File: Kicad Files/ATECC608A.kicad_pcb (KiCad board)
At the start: 2 copper layers, 7 parts, among them J1 Conn_01x04, U1 ATECC608A-SSHDA

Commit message: Change name LED1 and netlist
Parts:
- renumbered D1 to ON
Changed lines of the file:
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@@
-(kicad_pcb (version 20171130) (host pcbnew "(5.1.4-0-10_14)")
+(kicad_pcb (version 20171130) (host pcbnew "(5.1.4)-1")
   (general
     (thickness 1.6)
@@
     (solder_mask_min_width 0.25)
     (aux_axis_origin 0 0)
-    (visible_elements FFFFFF7F)
+    (visible_elements 7FFFFFFF)
     (pcbplotparams
       (layerselection 0x010fc_ffffffff)
@@
   (net 1 +3V3)
   (net 2 GND)
-  (net 3 "Net-(D1-Pad1)")
-  (net 4 /SCL)
-  (net 5 /SDA)
+  (net 3 /SCL)
+  (net 4 /SDA)
+  (net 5 "Net-(ON1-Pad1)")
   (net_class Default "This is the default net class."
     (clearance 0.2)
@@
     (add_net /SDA)
     (add_net GND)
-    (add_net "Net-(D1-Pad1)")
-  )
-  (module Capacitor_SMD:C_0805_2012Metric_Pad1.15x1.40mm_HandSolder (layer F.Cu)
-    (at 164.275 32.525 180)
-    (descr "Capacitor SMD 0805 (2012 Metric), square (rectangular) end terminal, IPC_7351 nominal with elongated pad for handsoldering. (Body size source: https://docs.google.com/spreadsheets/d/1BsfQQcO9C6DZCsRaXUlFlo91Tg2WpOkGARC1WS5S8t0/edit?usp=sharing), generated with kicad-footprint-generator")
-    (tags "capacitor handsolder")
-    (attr smd)
-    (fp_text reference C1 (at 0 -1.65) (layer F.SilkS)
-      (effects (font (size 1 1) (thickness 0.15)))
-    )
-    (fp_text value 0.1uF (at 0 1.65) (layer F.Fab)
-      (effects (font (size 1 1) (thickness 0.15)))
-    )
-    (fp_line (start -1 0.6) (end -1 -0.6) (layer F.Fab) (width 0.1))
-    (fp_line (start -1 -0.6) (end 1 -0.6) (layer F.Fab) (width 0.1))
-    (fp_line (start 1 -0.6) (end 1 0.6) (layer F.Fab) (width 0.1))
-    (fp_line (start 1 0.6) (end -1 0.6) (layer F.Fab) (width 0.1))
-    (fp_line (start -0.261252 -0.71) (end 0.261252 -0.71) (layer F.SilkS) (width 0.12))
-    (fp_line (start -0.261252 0.71) (end 0.261252 0.71) (layer F.SilkS) (width 0.12))
-    (fp_line (start -1.85 0.95) (end -1.85 -0.95) (layer F.CrtYd) (width 0.05))
-    (fp_line (start -1.85 -0.95) (end 1.85 -0.95) (layer F.CrtYd) (width 0.05))
-    (fp_line (start 1.85 -0.95) (end 1.85 0.95) (layer F.CrtYd) (width 0.05))
-    (fp_line (start 1.85 0.95) (end -1.85 0.95) (layer F.CrtYd) (width 0.05))
-    (fp_text user %R (at 0 0) (layer F.Fab)
-      (effects (font (size 0.5 0.5) (thickness 0.08)))
-    )
-    (pad 1 smd roundrect (at -1.025 0 180) (size 1.15 1.4) (layers F.Cu F.Paste F.Mask) (roundrect_rratio 0.217391)
-      (net 1 +3V3))
-    (pad 2 smd roundrect (at 1.025 0 180) (size 1.15 1.4) (layers F.Cu F.Paste F.Mask) (roundrect_rratio 0.217391)
-      (net 2 GND))
-    (model ${KISYS3DMOD}/Capacitor_SMD.3dshapes/C_0805_2012Metric.wrl
-      (at (xyz 0 0 0))
-      (scale (xyz 1 1 1))
-      (rotate (xyz 0 0 0))
-    )
+    (add_net "Net-(ON1-Pad1)")
   )
   (module LED_SMD:LED_0805_2012Metric_Pad1.15x1.40mm_HandSolder (layer F.Cu)
@@
     (tags "LED handsolder")
     (attr smd)
-    (fp_text reference D1 (at 0 -1.65) (layer F.SilkS)
+    (fp_text reference ON (at 0 -1.65) (layer F.SilkS)
       (effects (font (size 1 1) (thickness 0.15)))
     )
@@
     )
     (pad 1 smd roundrect (at -1.025 0) (size 1.15 1.4) (layers F.Cu F.Paste F.Mask) (roundrect_rratio 0.217391)
-      (net 3 "Net-(D1-Pad1)"))
+      (net 5 "Net-(ON1-Pad1)"))
     (pad 2 smd roundrect (at 1.025 0) (size 1.15 1.4) (layers F.Cu F.Paste F.Mask) (roundrect_rratio 0.217391)
       (net 1 +3V3))
     (model ${KISYS3DMOD}/LED_SMD.3dshapes/LED_0805_2012Metric.wrl
+      (at (xyz 0 0 0))
+      (scale (xyz 1 1 1))
+      (rotate (xyz 0 0 0))
+    )
+  )
+  (module Capacitor_SMD:C_0805_2012Metric_Pad1.15x1.40mm_HandSolder (layer F.Cu)
+    (at 164.275 32.525 180)
+    (descr "Capacitor SMD 0805 (2012 Metric), square (rectangular) end terminal, IPC_7351 nominal with elongated pad for handsoldering. (Body size source: https://docs.google.com/spreadsheets/d/1BsfQQcO9C6DZCsRaXUlFlo91Tg2WpOkGARC1WS5S8t0/edit?usp=sharing), generated with kicad-footprint-generator")
+    (tags "capacitor handsolder")
+    (attr smd)
+    (fp_text reference C1 (at 0 -1.65) (layer F.SilkS)
+      (effects (font (size 1 1) (thickness 0.15)))
+    )
+    (fp_text value 0.1uF (at 0 1.65) (layer F.Fab)
+      (effects (font (size 1 1) (thickness 0.15)))
+    )
+    (fp_line (start -1 0.6) (end -1 -0.6) (layer F.Fab) (width 0.1))
+    (fp_line (start -1 -0.6) (end 1 -0.6) (layer F.Fab) (width 0.1))
+    (fp_line (start 1 -0.6) (end 1 0.6) (layer F.Fab) (width 0.1))
+    (fp_line (start 1 0.6) (end -1 0.6) (layer F.Fab) (width 0.1))
+    (fp_line (start -0.261252 -0.71) (end 0.261252 -0.71) (layer F.SilkS) (width 0.12))
+    (fp_line (start -0.261252 0.71) (end 0.261252 0.71) (layer F.SilkS) (width 0.12))
+    (fp_line (start -1.85 0.95) (end -1.85 -0.95) (layer F.CrtYd) (width 0.05))
+    (fp_line (start -1.85 -0.95) (end 1.85 -0.95) (layer F.CrtYd) (width 0.05))
+    (fp_line (start 1.85 -0.95) (end 1.85 0.95) (layer F.CrtYd) (width 0.05))
+    (fp_line (start 1.85 0.95) (end -1.85 0.95) (layer F.CrtYd) (width 0.05))
+    (fp_text user %R (at 0 0) (layer F.Fab)
+      (effects (font (size 0.5 0.5) (thickness 0.08)))
+    )
+    (pad 1 smd roundrect (at -1.025 0 180) (size 1.15 1.4) (layers F.Cu F.Paste F.Mask) (roundrect_rratio 0.217391)
+      (net 1 +3V3))
+    (pad 2 smd roundrect (at 1.025 0 180) (size 1.15 1.4) (layers F.Cu F.Paste F.Mask) (roundrect_rratio 0.217391)
+      (net 2 GND))
+    (model ${KISYS3DMOD}/Capacitor_SMD.3dshapes/C_0805_2012Metric.wrl
       (at (xyz 0 0 0))
       (scale (xyz 1 1 1))
@@
       (net 2 GND))
     (pad 3 thru_hole oval (at 0 5.08 90) (size 1.7 1.7) (drill 1) (layers *.Cu *.Mask)
-      (net 4 /SCL))
+      (net 3 /SCL))
     (pad 4 thru_hole oval (at 0 7.62 90) (size 1.7 1.7) (drill 1) (layers *.Cu *.Mask)
-      (net 5 /SDA))
+      (net 4 /SDA))
     (model ${KISYS3DMOD}/Connector_PinHeader_2.54mm.3dshapes/PinHeader_1x04_P2.54mm_Vertical.wrl
       (at (xyz 0 0 0))
@@
     )
     (pad 1 smd roundrect (at -1.025 0) (size 1.15 1.4) (layers F.Cu F.Paste F.Mask) (roundrect_rratio 0.217391)
-      (net 3 "Net-(D1-Pad1)"))
+      (net 5 "Net-(ON1-Pad1)"))
     (pad 2 smd roundrect (at 1.025 0) (size 1.15 1.4) (layers F.Cu F.Paste F.Mask) (roundrect_rratio 0.217391)
       (net 2 GND))
@@
       (net 2 GND))
     (pad 5 smd roundrect (at 2.475 1.905) (size 1.95 0.6) (layers F.Cu F.Paste F.Mask) (roundrect_rratio 0.25)
-      (net 5 /SDA))
+      (net 4 /SDA))
     (pad 6 smd roundrect (at 2.475 0.635) (size 1.95 0.6) (layers F.Cu F.Paste F.Mask) (roundrect_rratio 0.25)
-      (net 4 /SCL))
+      (net 3 /SCL))
     (pad 7 smd roundrect (at 2.475 -0.635) (size 1.95 0.6) (layers F.Cu F.Paste F.Mask) (roundrect_rratio 0.25))
     (pad 8 smd roundrect (at 2.475 -1.905) (size 1.95 0.6) (layers F.Cu F.Paste F.Mask) (roundrect_rratio 0.25)
@@
     (fp_line (start -1 0.6) (end -1 -0.6) (layer F.Fab) (width 0.1))
     (pad 2 smd roundrect (at 1.025 0 270) (size 1.15 1.4) (layers F.Cu F.Paste F.Mask) (roundrect_rratio 0.217391)
-      (net 4 /SCL))
+      (net 3 /SCL))
     (pad 1 smd roundrect (at -1.025 0 270) (size 1.15 1.4) (layers F.Cu F.Paste F.Mask) (roundrect_rratio 0.217391)
       (net 1 +3V3))
@@
       (net 1 +3V3))
     (pad 2 smd roundrect (at 1.025 0 270) (size 1.15 1.4) (layers F.Cu F.Paste F.Mask) (roundrect_rratio 0.217391)
-      (net 5 /SDA))
+      (net 4 /SDA))
     (model ${KISYS3DMOD}/Resistor_SMD.3dshapes/R_0805_2012Metric.wrl
       (at (xyz 0 0 0))

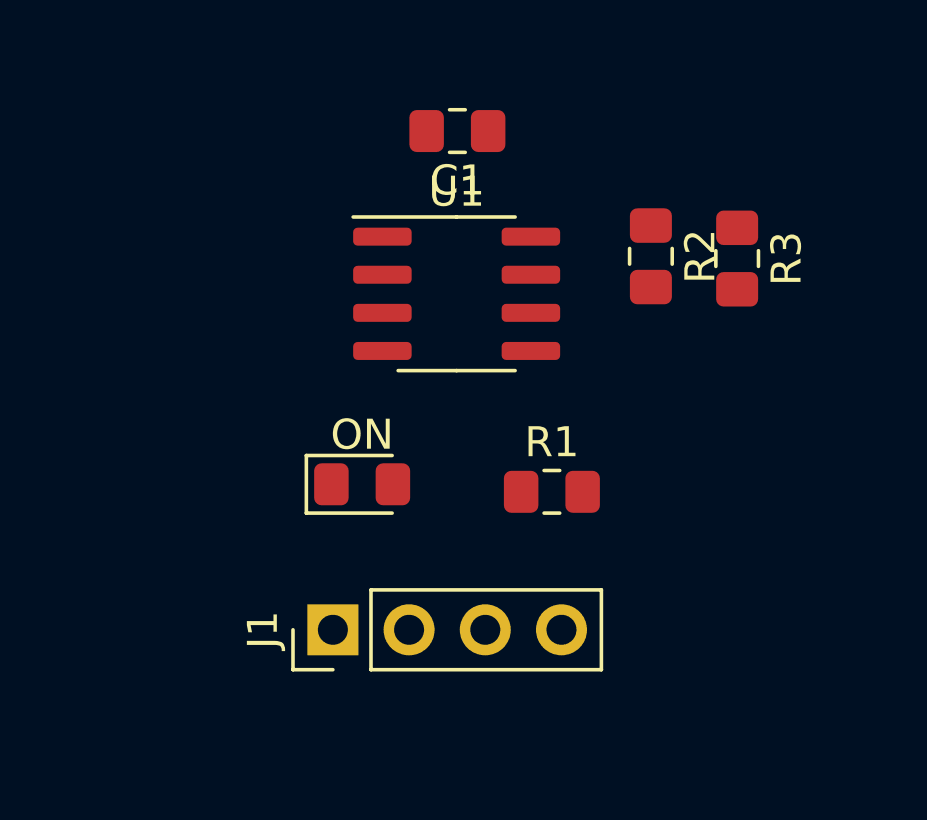
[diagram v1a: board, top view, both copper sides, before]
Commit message: Desing rules and  contour pcb
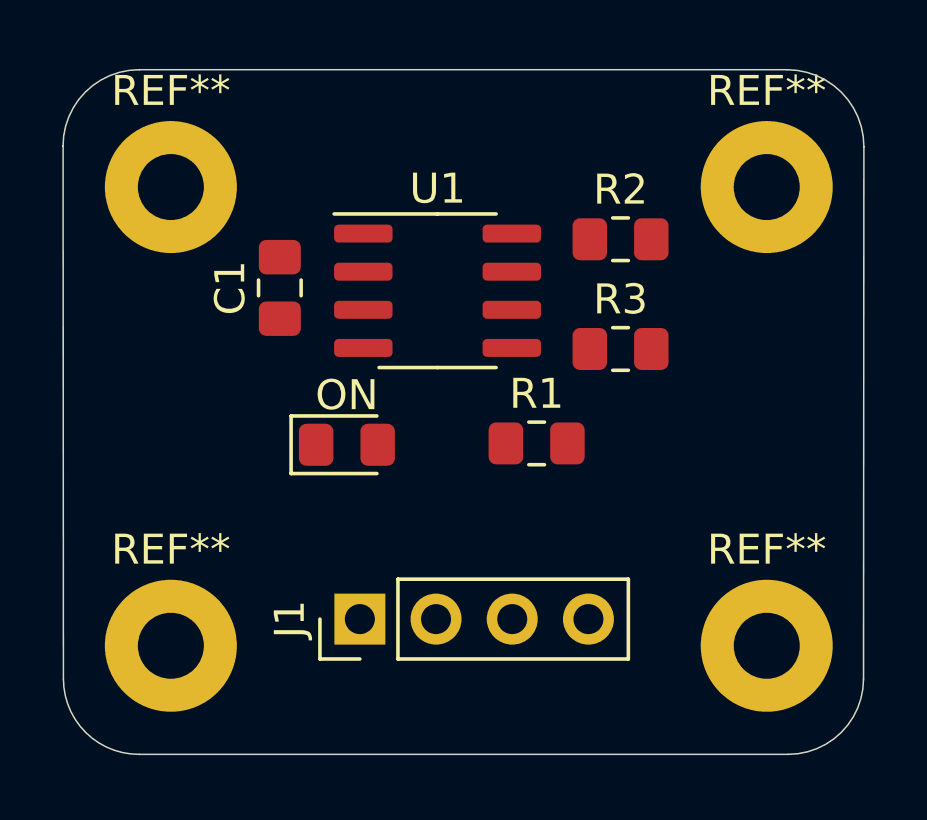
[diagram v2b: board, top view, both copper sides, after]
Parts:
- added REF**: MountingHole_2.2mm_M2_Pad, MountingHole:MountingHole_2.2mm_M2_Pad, F.Cu at (154.7, 34.4)
- added REF**: MountingHole_2.2mm_M2_Pad, MountingHole:MountingHole_2.2mm_M2_Pad, F.Cu at (154.7, 49.7)
- added REF**: MountingHole_2.2mm_M2_Pad, MountingHole:MountingHole_2.2mm_M2_Pad, F.Cu at (174.6, 49.7)
- added REF**: MountingHole_2.2mm_M2_Pad, MountingHole:MountingHole_2.2mm_M2_Pad, F.Cu at (174.6, 34.4)
- moved C1 7.90 mm to (158.4, 37.8), turned to 90 degrees
- moved R3 4.92 mm to (169.7, 39.8), turned to 0 degrees
- moved R1 1.69 mm to (166.9, 42.9)
- moved ON 1.41 mm to (160.6, 43.0)
- moved R2 1.16 mm to (169.7, 36.1), turned to 0 degrees
- moved J1 0.97 mm to (161.0, 48.8)
- moved U1 0.64 mm to (163.6, 37.8)
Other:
- board outline added: 26.7 x 22.8 mm
- net class Default: clearance 0.2 -> 0.25; trace_width 0.25 -> 0.3
- net class vcc added: clearance 0.45, trace_width 0.5, via_dia 0.8, via_drill 0.4
- rule trace_clearance: 0.2 -> 0.25

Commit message: add logo EC
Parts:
- added G***: LOGO, Aesthetics:electronic_cats_logo_8x6, F.Cu at (173.5, 43.4)
- moved C1 2.09 mm to (159.7, 39.4)
- moved R1 2.09 mm to (168.3, 44.5)
- moved R3 2.09 mm to (171.1, 41.4)
- moved ON 2.09 mm to (161.9, 44.6)
- moved R2 2.09 mm to (171.1, 37.7)
- moved U1 2.09 mm to (165.0, 39.4)
- moved J1 0.99 mm to (161.0, 49.8)

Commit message: Change of measures
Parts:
- moved REF** 0.20 mm to (174.5, 49.5)
- moved REF** 0.19 mm to (174.6, 34.2)
- moved REF** 0.18 mm to (154.7, 34.2)
- moved REF** 0.14 mm to (154.9, 49.7)

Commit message: accommodation screws
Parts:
- moved REF** 0.27 mm to (154.9, 49.5)
- moved REF** 0.07 mm to (174.4, 49.5)
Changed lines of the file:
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@@
   )
   (module MountingHole:MountingHole_2.2mm_M2_Pad (layer F.Cu)
-    (at 154.8511 49.7459)
+    (at 154.8638 49.4792)
     (descr "Mounting Hole 2.2mm, M2")
     (tags "mounting hole 2.2mm m2")
@@
   )
   (module MountingHole:MountingHole_2.2mm_M2_Pad (layer F.Cu)
-    (at 174.4726 49.5173)
+    (at 174.4091 49.4919)
     (descr "Mounting Hole 2.2mm, M2")
     (tags "mounting hole 2.2mm m2")
@@
     )
   )
+  (dimension 3.8481 (width 0.15) (layer Margin)
+    (gr_text "3.848 mm" (at 181.9067 51.41595 90) (layer Margin)
+      (effects (font (size 1 1) (thickness 0.15)))
+    )
+    (feature1 (pts (xy 174.2059 49.4919) (xy 181.193121 49.4919)))
+    (feature2 (pts (xy 174.2059 53.34) (xy 181.193121 53.34)))
+    (crossbar (pts (xy 180.6067 53.34) (xy 180.6067 49.4919)))
+    (arrow1a (pts (xy 180.6067 49.4919) (xy 181.193121 50.618404)))
+    (arrow1b (pts (xy 180.6067 49.4919) (xy 180.020279 50.618404)))
+    (arrow2a (pts (xy 180.6067 53.34) (xy 181.193121 52.213496)))
+    (arrow2b (pts (xy 180.6067 53.34) (xy 180.020279 52.213496)))
+  )
+  (dimension 3.8481 (width 0.15) (layer Margin)
+    (gr_text "3.848 mm" (at 146.401 51.37785 90) (layer Margin)
+      (effects (font (size 1 1) (thickness 0.15)))
+    )
+    (feature1 (pts (xy 154.9019 49.4538) (xy 147.114579 49.4538)))
+    (feature2 (pts (xy 154.9019 53.3019) (xy 147.114579 53.3019)))
+    (crossbar (pts (xy 147.701 53.3019) (xy 147.701 49.4538)))
+    (arrow1a (pts (xy 147.701 49.4538) (xy 148.287421 50.580304)))
+    (arrow1b (pts (xy 147.701 49.4538) (xy 147.114579 50.580304)))
+    (arrow2a (pts (xy 147.701 53.3019) (xy 148.287421 52.175396)))
+    (arrow2b (pts (xy 147.701 53.3019) (xy 147.114579 52.175396)))
+  )
   (dimension 3.7211 (width 0.15) (layer Margin)
     (gr_text "3.721 mm" (at 153.02865 59.3517) (layer Margin)
@@
     (arrow2b (pts (xy 154.9146 25.8064) (xy 153.788096 26.392821)))
   )
-  (dimension 3.7084 (width 0.15) (layer Margin)
-    (gr_text "3.708 mm" (at 181.2209 51.3969 270) (layer Margin)
-      (effects (font (size 1 1) (thickness 0.15)))
-    )
-    (feature1 (pts (xy 174.4853 53.2511) (xy 180.507321 53.2511)))
-    (feature2 (pts (xy 174.4853 49.5427) (xy 180.507321 49.5427)))
-    (crossbar (pts (xy 179.9209 49.5427) (xy 179.9209 53.2511)))
-    (arrow1a (pts (xy 179.9209 53.2511) (xy 179.334479 52.124596)))
-    (arrow1b (pts (xy 179.9209 53.2511) (xy 180.507321 52.124596)))
-    (arrow2a (pts (xy 179.9209 49.5427) (xy 179.334479 50.669204)))
-    (arrow2b (pts (xy 179.9209 49.5427) (xy 180.507321 50.669204)))
-  )
-  (dimension 3.7592 (width 0.15) (layer Margin)
-    (gr_text "3.759 mm" (at 145.131 51.3715 270) (layer Margin)
-      (effects (font (size 1 1) (thickness 0.15)))
-    )
-    (feature1 (pts (xy 154.9019 53.2511) (xy 145.844579 53.2511)))
-    (feature2 (pts (xy 154.9019 49.4919) (xy 145.844579 49.4919)))
-    (crossbar (pts (xy 146.431 49.4919) (xy 146.431 53.2511)))
-    (arrow1a (pts (xy 146.431 53.2511) (xy 145.844579 52.124596)))
-    (arrow1b (pts (xy 146.431 53.2511) (xy 147.017421 52.124596)))
-    (arrow2a (pts (xy 146.431 49.4919) (xy 145.844579 50.618404)))
-    (arrow2b (pts (xy 146.431 49.4919) (xy 147.017421 50.618404)))
-  )
   (dimension 3.8481 (width 0.15) (layer Margin)

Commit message: initial routeo
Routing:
- net /SCL: track 0.00 -> 34.2 mm, vias 0 -> 1
- net +3V3: track 0.00 -> 32.7 mm
- net /SDA: track 0.00 -> 16.5 mm
- net Net-(ON1-Pad1): track 0.00 -> 9.09 mm
- added copper zone on B.Cu, net GND
- added copper zone on F.Cu, net GND
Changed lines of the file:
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@@
     (thickness 1.6)
     (drawings 21)
-    (tracks 0)
+    (tracks 64)
     (zones 0)
     (modules 12)
@@
   (gr_arc (start 153.67 33.02) (end 153.67 30.48) (angle -90) (layer Edge.Cuts) (width 0.05))
   (gr_arc (start 175.26 33.0454) (end 177.8254 33.0454) (angle -90) (layer Edge.Cuts) (width 0.05))
+  (segment (start 169.850701 37.543401) (end 170.0388 37.7315) (width 0.3) (layer F.Cu) (net 1))
+  (segment (start 167.440001 37.543401) (end 169.850701 37.543401) (width 0.3) (layer F.Cu) (net 1))
+  (segment (start 159.886 49.784) (end 161.036 49.784) (width 0.3) (layer F.Cu) (net 1))
+  (segment (start 159.7063 49.6043) (end 159.886 49.784) (width 0.3) (layer F.Cu) (net 1))
+  (segment (start 162.967 44.5821) (end 162.967 43.0409) (width 0.3) (layer F.Cu) (net 1))
+  (segment (start 162.967 43.0409) (end 162.6578 42.7317) (width 0.3) (layer F.Cu) (net 1))
+  (segment (start 160.0035 42.7317) (end 159.7063 42.4345) (width 0.3) (layer F.Cu) (net 1))
+  (segment (start 160.067 42.7317) (end 160.0035 42.7317) (width 0.3) (layer F.Cu) (net 1))
+  (segment (start 159.7063 42.4345) (end 159.7063 42.7317) (width 0.3) (layer F.Cu) (net 1))
+  (segment (start 159.7063 40.3784) (end 159.7063 42.4345) (width 0.3) (layer F.Cu) (net 1))
+  (segment (start 160.067 42.7317) (end 159.7063 42.7317) (width 0.3) (layer F.Cu) (net 1))
+  (segment (start 159.9552 42.7317) (end 159.7063 42.9806) (width 0.3) (layer F.Cu) (net 1))
+  (segment (start 160.067 42.7317) (end 159.9552 42.7317) (width 0.3) (layer F.Cu) (net 1))
+  (segment (start 159.7063 42.7317) (end 159.7063 42.9806) (width 0.3) (layer F.Cu) (net 1))
+  (segment (start 159.7063 42.9806) (end 159.7063 49.6043) (width 0.3) (layer F.Cu) (net 1))
+  (segment (start 166.365001 37.543401) (end 165.0619 38.846502) (width 0.3) (layer F.Cu) (net 1))
+  (segment (start 167.440001 37.543401) (end 166.365001 37.543401) (width 0.3) (layer F.Cu) (net 1))
+  (segment (start 165.0619 38.846502) (end 165.0619 42.4434) (width 0.3) (layer F.Cu) (net 1))
+  (segment (start 165.0619 42.4434) (end 164.7736 42.7317) (width 0.3) (layer F.Cu) (net 1))
+  (segment (start 162.6578 42.7317) (end 162.3098 42.7317) (width 0.3) (layer F.Cu) (net 1))
+  (segment (start 162.3098 42.7317) (end 160.067 42.7317) (width 0.3) (layer F.Cu) (net 1))
+  (segment (start 162.9963 43.0409) (end 163.3055 42.7317) (width 0.3) (layer F.Cu) (net 1))
+  (segment (start 162.967 43.0409) (end 162.9963 43.0409) (width 0.3) (layer F.Cu) (net 1))
+  (segment (start 164.7736 42.7317) (end 163.3055 42.7317) (width 0.3) (layer F.Cu) (net 1))
+  (segment (start 163.3055 42.7317) (end 162.3098 42.7317) (width 0.3) (layer F.Cu) (net 1))
+  (segment (start 170.0388 40.5891) (end 170.0388 37.7315) (width 0.3) (layer F.Cu) (net 1))
+  (segment (start 170.0388 41.3891) (end 170.0388 40.5891) (width 0.3) (layer F.Cu) (net 1))
+  (via (at 166.1033 42.8498) (size 0.8) (drill 0.4) (layers F.Cu B.Cu) (net 3))
+  (segment (start 166.116 49.784) (end 166.116 42.8625) (width 0.3) (layer B.Cu) (net 3))
+  (segment (start 166.116 42.8625) (end 166.1033 42.8498) (width 0.3) (layer B.Cu) (net 3))
+  (segment (start 166.365001 40.083401) (end 167.440001 40.083401) (width 0.3) (layer F.Cu) (net 3))
+  (segment (start 166.064991 40.383411) (end 166.365001 40.083401) (width 0.3) (layer F.Cu) (net 3))
+  (segment (start 166.064991 41.731225) (end 166.064991 40.383411) (width 0.3) (layer F.Cu) (net 3))
+  (segment (start 166.1033 41.769534) (end 166.064991 41.731225) (width 0.3) (layer F.Cu) (net 3))
+  (segment (start 166.1033 42.8498) (end 166.1033 41.769534) (width 0.3) (layer F.Cu) (net 3))
+  (segment (start 172.7638 37.7315) (end 173.4566 38.4243) (width 0.3) (layer F.Cu) (net 3))
+  (segment (start 172.0888 37.7315) (end 172.7638 37.7315) (width 0.3) (layer F.Cu) (net 3))
+  (segment (start 173.4566 38.4243) (end 173.4566 45.2247) (width 0.3) (layer F.Cu) (net 3))
+  (segment (start 173.4566 45.2247) (end 170.7261 47.9552) (width 0.3) (layer F.Cu) (net 3))
+  (segment (start 170.7261 47.9552) (end 170.7261 51.8541) (width 0.3) (layer F.Cu) (net 3))
+  (segment (start 170.7261 51.8541) (end 170.2562 52.324) (width 0.3) (layer F.Cu) (net 3))
+  (segment (start 170.2562 52.324) (end 166.6367 52.324) (width 0.3) (layer F.Cu) (net 3))
+  (segment (start 166.116 51.8033) (end 166.116 49.784) (width 0.3) (layer F.Cu) (net 3))
+  (segment (start 166.6367 52.324) (end 166.116 51.8033) (width 0.3) (layer F.Cu) (net 3))
+  (segment (start 172.0888 42.1891) (end 172.0888 41.3891) (width 0.3) (layer F.Cu) (net 4))
+  (segment (start 168.656 48.581919) (end 172.0888 45.149119) (width 0.3) (layer F.Cu) (net 4))
+  (segment (start 168.656 49.784) (end 168.656 48.581919) (width 0.3) (layer F.Cu) (net 4))
+  (segment (start 167.440001 41.753401) (end 168.7485 43.0619) (width 0.3) (layer F.Cu) (net 4))
+  (segment (start 167.440001 41.353401) (end 167.440001 41.753401) (width 0.3) (layer F.Cu) (net 4))
+  (segment (start 171.8551 43.0619) (end 172.0888 42.8282) (width 0.3) (layer F.Cu) (net 4))
+  (segment (start 171.6443 43.0619) (end 171.8551 43.0619) (width 0.3) (layer F.Cu) (net 4))
+  (segment (start 172.0888 42.8282) (end 172.0888 42.1891) (width 0.3) (layer F.Cu) (net 4))
+  (segment (start 172.0888 43.0619) (end 172.0888 42.8282) (width 0.3) (layer F.Cu) (net 4))
+  (segment (start 171.6443 43.0619) (end 172.0888 43.0619) (width 0.3) (layer F.Cu) (net 4))
+  (segment (start 168.7485 43.0619) (end 171.6443 43.0619) (width 0.3) (layer F.Cu) (net 4))
+  (segment (start 171.8221 43.0619) (end 172.0888 43.3286) (width 0.3) (layer F.Cu) (net 4))
+  (segment (start 171.6443 43.0619) (end 171.8221 43.0619) (width 0.3) (layer F.Cu) (net 4))
+  (segment (start 172.0888 45.149119) (end 172.0888 43.3286) (width 0.3) (layer F.Cu) (net 4))
+  (segment (start 172.0888 43.3286) (end 172.0888 43.0619) (width 0.3) (layer F.Cu) (net 4))
+  (segment (start 160.917 44.5821) (end 160.917 45.728) (width 0.3) (layer F.Cu) (net 5))
+  (segment (start 160.917 45.728) (end 161.3916 46.2026) (width 0.3) (layer F.Cu) (net 5))
+  (segment (start 161.3916 46.2026) (end 166.8272 46.2026) (width 0.3) (layer F.Cu) (net 5))
+  (segment (start 167.242 45.7878) (end 167.242 44.5371) (width 0.3) (layer F.Cu) (net 5))
+  (segment (start 166.8272 46.2026) (end 167.242 45.7878) (width 0.3) (layer F.Cu) (net 5))
+  (zone (net 2) (net_name GND) (layer F.Cu) (hatch edge 0.508)
+    (connect_pads (clearance 0.508))
+    (min_thickness 0.254)
+    (fill yes (arc_segments 32) (thermal_gap 0.508) (thermal_bridge_width 0.508))
+    (polygon
+      (pts
+        (xy 151.2062 30.5054) (xy 177.8635 30.4673) (xy 177.8 53.3654) (xy 151.1427 53.3273)
+      )
+    )
+  )
+  (zone (net 2) (net_name GND) (layer B.Cu) (hatch edge 0.508)
+    (connect_pads (clearance 0.508))
+    (min_thickness 0.254)
+    (fill yes (arc_segments 32) (thermal_gap 0.508) (thermal_bridge_width 0.508))
+    (polygon
+      (pts
+        (xy 151.13 30.5435) (xy 177.927 30.4419) (xy 177.8762 53.4797) (xy 151.0792 53.3781)
+      )
+    )
+  )
 )
